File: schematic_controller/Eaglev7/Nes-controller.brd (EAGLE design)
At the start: 110.2 x 55.9 mm, 38 parts

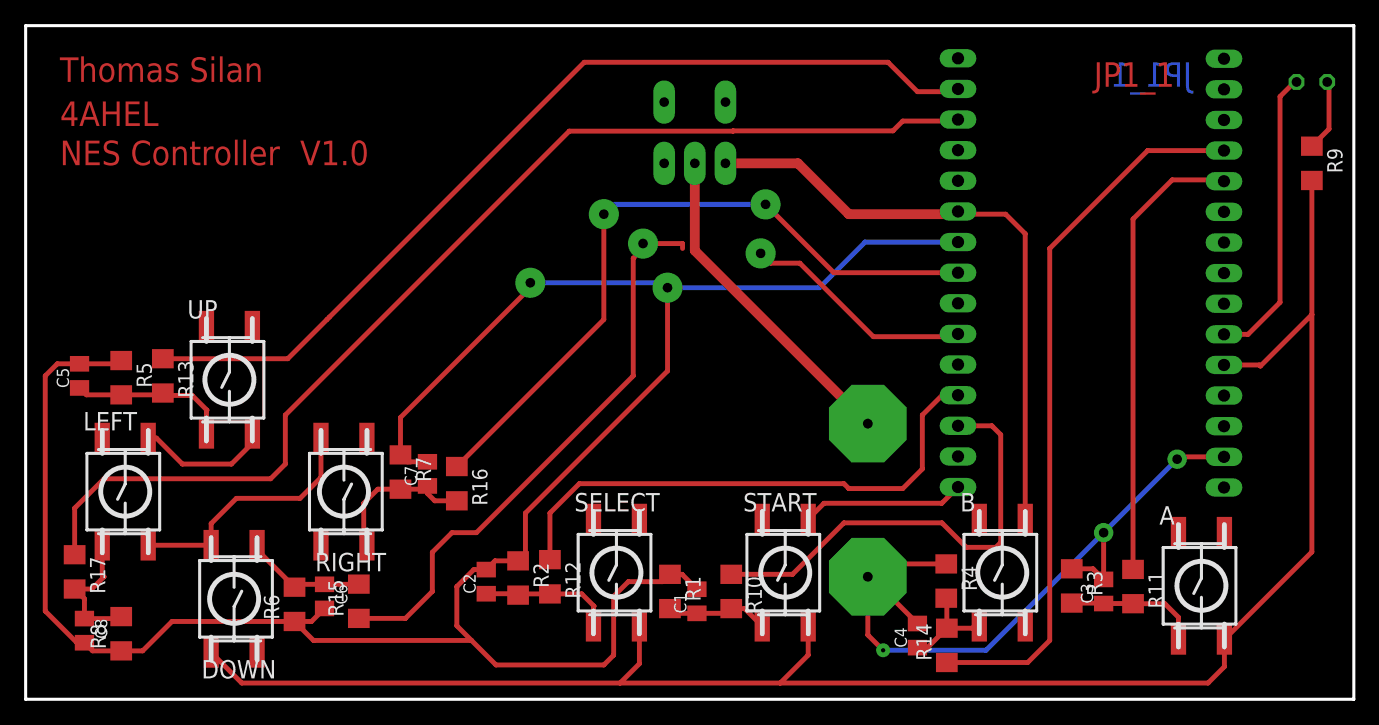
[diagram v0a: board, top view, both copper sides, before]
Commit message: added schematic and board for eaglev7
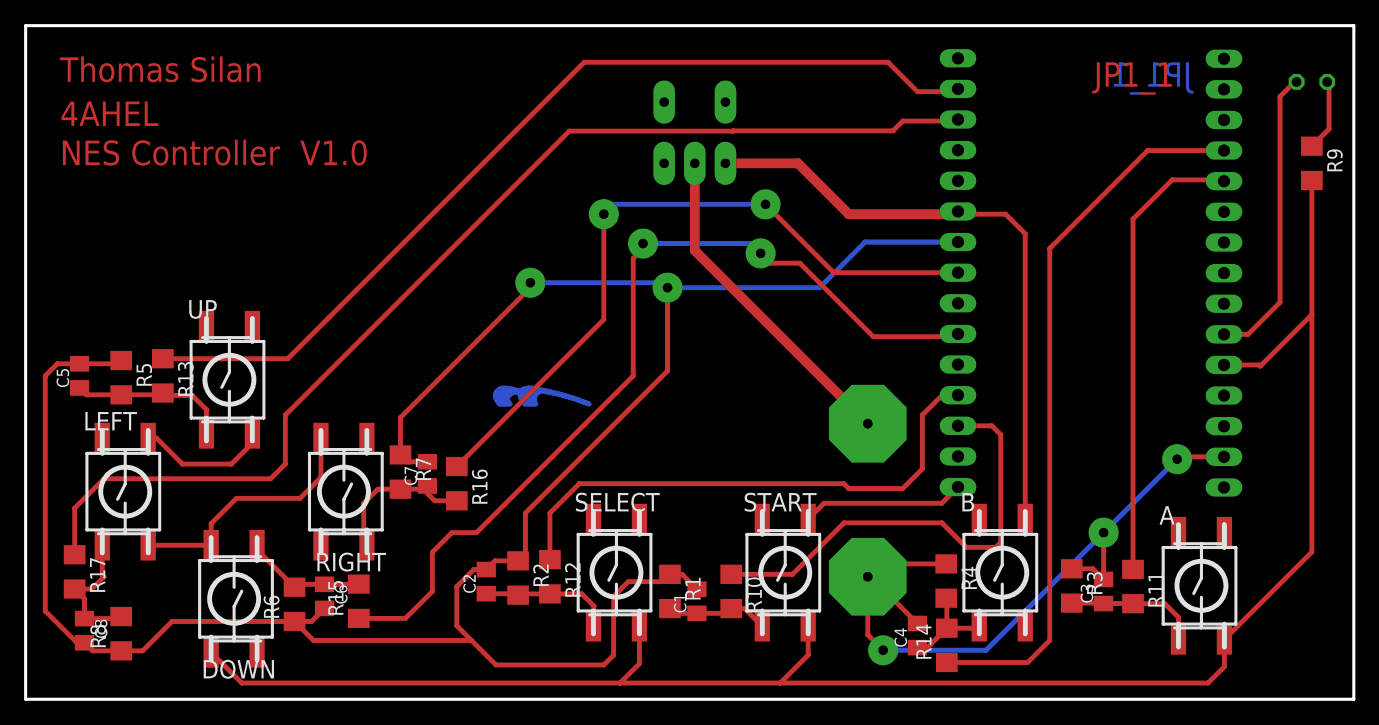
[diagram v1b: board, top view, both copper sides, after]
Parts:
- added E$1: (no value), HTL-Logo:LOGOBOT_8
- C1, C2, C3, C4, C5, C6, C7, C8: device rcl:C0805K -> rcl@1:C0805K
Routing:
- net DOWN: track 67.3 -> 73.7 mm
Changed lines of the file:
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@@
 <?xml version="1.0" encoding="utf-8"?>
 <!DOCTYPE eagle SYSTEM "eagle.dtd">
-<eagle version="8.5.0">
+<eagle version="7.7.0">
 <drawing>
 <settings>
@@
 <element name="UP" library="Schalter-sh" package="SMDTAST" value="" x="16.9" y="26.5"/>
 <element name="R10" library="rcl" package="R1206" value="" x="58.5216" y="8.9408" rot="R270"/>
-<element name="C1" library="rcl" library_urn="urn:adsk.eagle:library:334" package="C0805K" package3d_urn="urn:adsk.eagle:package:23681/2" value="" x="55.6768" y="8.128" rot="R90">
+<element name="C1" library="rcl@1" package="C0805K" value="" x="55.6768" y="8.128" rot="R90">
 <attribute name="SPICEPREFIX" value="C" x="55.6768" y="8.128" size="1.778" layer="27" rot="R90" display="off"/>
 </element>
 <element name="R11" library="rcl" package="R1206" value="" x="91.8464" y="9.3472" rot="R270"/>
 <element name="R12" library="rcl" package="R1206" value="" x="43.4848" y="10.16" rot="R270"/>
-<element name="C2" library="rcl" library_urn="urn:adsk.eagle:library:334" package="C0805K" package3d_urn="urn:adsk.eagle:package:23681/2" value="" x="38.2016" y="9.7536" rot="R90">
+<element name="C2" library="rcl@1" package="C0805K" value="" x="38.2016" y="9.7536" rot="R90">
 <attribute name="SPICEPREFIX" value="C" x="38.2016" y="9.7536" size="1.778" layer="27" rot="R90" display="off"/>
 </element>
-<element name="C3" library="rcl" library_urn="urn:adsk.eagle:library:334" package="C0805K" package3d_urn="urn:adsk.eagle:package:23681/2" value="" x="89.408" y="8.9408" rot="R90">
+<element name="C3" library="rcl@1" package="C0805K" value="" x="89.408" y="8.9408" rot="R90">
 <attribute name="SPICEPREFIX" value="C" x="89.408" y="8.9408" size="1.778" layer="27" rot="R90" display="off"/>
 </element>
 <element name="R14" library="rcl" package="R1206" value="" x="76.4032" y="4.4704" rot="R90"/>
-<element name="C4" library="rcl" library_urn="urn:adsk.eagle:library:334" package="C0805K" package3d_urn="urn:adsk.eagle:package:23681/2" value="" x="73.9648" y="5.2832" rot="R90">
+<element name="C4" library="rcl@1" package="C0805K" value="" x="73.9648" y="5.2832" rot="R90">
 <attribute name="SPICEPREFIX" value="C" x="73.9648" y="5.2832" size="1.778" layer="27" rot="R90" display="off"/>
 </element>
 <element name="R13" library="rcl" package="R1206" value="" x="11.3792" y="26.8224" rot="R270"/>
-<element name="C5" library="rcl" library_urn="urn:adsk.eagle:library:334" package="C0805K" package3d_urn="urn:adsk.eagle:package:23681/2" value="" x="4.4704" y="26.8224" rot="R90">
+<element name="C5" library="rcl@1" package="C0805K" value="" x="4.4704" y="26.8224" rot="R90">
 <attribute name="SPICEPREFIX" value="C" x="4.4704" y="26.8224" size="1.778" layer="27" rot="R90" display="off"/>
 </element>
 <element name="R15" library="rcl" package="R1206" value="" x="27.6352" y="8.128" rot="R90"/>
-<element name="C6" library="rcl" library_urn="urn:adsk.eagle:library:334" package="C0805K" package3d_urn="urn:adsk.eagle:package:23681/2" value="" x="24.7904" y="8.5344" rot="R270">
+<element name="C6" library="rcl@1" package="C0805K" value="" x="24.7904" y="8.5344" rot="R270">
 <attribute name="SPICEPREFIX" value="C" x="24.7904" y="8.5344" size="1.778" layer="27" rot="R270" display="off"/>
 </element>
 <element name="R16" library="rcl" package="R1206" value="" x="35.7632" y="17.8816" rot="R270"/>
-<element name="C7" library="rcl" library_urn="urn:adsk.eagle:library:334" package="C0805K" package3d_urn="urn:adsk.eagle:package:23681/2" value="" x="33.3248" y="18.6944" rot="R90">
+<element name="C7" library="rcl@1" package="C0805K" value="" x="33.3248" y="18.6944" rot="R90">
 <attribute name="SPICEPREFIX" value="C" x="33.3248" y="18.6944" size="1.778" layer="27" rot="R90" display="off"/>
 </element>
 <element name="R17" library="rcl" package="R1206" value="" x="4.064" y="10.5664" rot="R270"/>
-<element name="C8" library="rcl" library_urn="urn:adsk.eagle:library:334" package="C0805K" package3d_urn="urn:adsk.eagle:package:23681/2" value="" x="4.8768" y="5.6896" rot="R270">
+<element name="C8" library="rcl@1" package="C0805K" value="" x="4.8768" y="5.6896" rot="R270">
 <attribute name="SPICEPREFIX" value="C" x="4.8768" y="5.6896" size="1.778" layer="27" rot="R270" display="off"/>
 </element>
+<element name="E$1" library="HTL-Logo" package="LOGOBOT_8" value="" x="43.0784" y="24.384"/>
 </elements>
 <signals>
@@
 <wire x1="88.5288" y1="10.82" x2="89.408" y2="9.9408" width="0.4064" layer="1"/>
 <wire x1="89.408" y1="9.9408" x2="89.408" y2="13.8176" width="0.4064" layer="1"/>
-<via x="89.408" y="13.8176" extent="1-16" drill="0.8" shape="octagon"/>
-<via x="95.504" y="19.9136" extent="1-16" drill="0.8" shape="octagon"/>
+<via x="89.408" y="13.8176" extent="1-16" drill="0.8" diameter="2.5" shape="octagon"/>
+<via x="95.504" y="19.9136" extent="1-16" drill="0.8" diameter="2.5" shape="octagon"/>
 <wire x1="89.408" y1="13.8176" x2="95.504" y2="19.9136" width="0.4064" layer="16"/>
 <wire x1="95.504" y1="19.9136" x2="95.6968" y2="20.1064" width="0.4064" layer="1"/>
@@
 <wire x1="69.85" y1="10.16" x2="69.85" y2="5.334" width="0.4064" layer="1"/>
 <wire x1="69.85" y1="5.334" x2="71.12" y2="4.064" width="0.4064" layer="1"/>
-<via x="71.12" y="4.064" extent="1-16" drill="0.35"/>
+<via x="71.12" y="4.064" extent="1-16" drill="0.8" diameter="2.5" shape="octagon"/>
 <wire x1="71.12" y1="4.064" x2="79.6544" y2="4.064" width="0.4064" layer="16"/>
 <wire x1="79.6544" y1="4.064" x2="89.408" y2="13.8176" width="0.4064" layer="16"/>
@@
 <wire x1="51.2064" y1="37.3888" x2="51.2064" y2="37.7952" width="0.4064" layer="1"/>
 <wire x1="50.3936" y1="26.8224" x2="50.3936" y2="36.576" width="0.4064" layer="1"/>
+<wire x1="51.2064" y1="37.7952" x2="60.1472" y2="37.7952" width="0.4064" layer="16"/>
+<wire x1="60.1472" y1="37.7952" x2="60.96" y2="36.9824" width="0.4064" layer="16"/>
+<wire x1="64.2112" y1="36.1696" x2="61.7728" y2="36.1696" width="0.4064" layer="1"/>
 <wire x1="61.7728" y1="36.1696" x2="60.96" y2="36.9824" width="0.4064" layer="1"/>
-<wire x1="64.2112" y1="36.1696" x2="61.7728" y2="36.1696" width="0.4064" layer="1"/>
-<wire x1="51.2064" y1="37.7952" x2="54.484" y2="37.7952" width="0.4064" layer="1"/>
-<wire x1="54.484" y1="37.7952" x2="54.484" y2="37.3888" width="0.4064" layer="1"/>
-<wire x1="54.484" y1="37.3888" x2="60.96" y2="36.9824" width="0" layer="19" extent="1-1"/>
 </signal>
 <signal name="RIGHT">
@@
 </board>
 </drawing>
-<compatibility>
-<note version="8.2" severity="warning">
-Since Version 8.2, EAGLE supports online libraries. The ids
-of those online libraries will not be understood (or retained)
-with this version.
-</note>
-<note version="8.3" severity="warning">
-Since Version 8.3, EAGLE supports URNs for individual library
-assets (packages, symbols, and devices). The URNs of those assets
-will not be understood (or retained) with this version.
-</note>
-<note version="8.3" severity="warning">
-Since Version 8.3, EAGLE supports the association of 3D packages
-with devices in libraries, schematics, and board files. Those 3D
-packages will not be understood (or retained) with this version.
-</note>
-</compatibility>
 </eagle>
